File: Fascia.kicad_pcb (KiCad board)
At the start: 6 copper layers, 148.2 x 64.3 mm, 118 parts, among them J1 Verdin iMX95, J10 RTC coin cell, J2 Power in, J3 CAN to ECU, J4 Panel LVDS (provisional), J5 Pre-outs to amp, J6 Mic, J7 USB-C CarPlay, J8 JTAG debug, J9 Buttons, Q1 NFET diode, Q2 NFET pass, Q3 NFET i2c xlat, Q4 NFET i2c xlat, U1 LM74930-Q1, U10 TPS2557-Q1, U2 LM61460-Q1, U3 TLV767-Q1, U4 TCAN1044V-Q1, U5 SN65DSI85-Q1, U6 TLV767-Q1 3V3, U7 SN74AXC4T245-Q1, U8 SN74AXC4T245-Q1, U9 PCM3168A-Q1

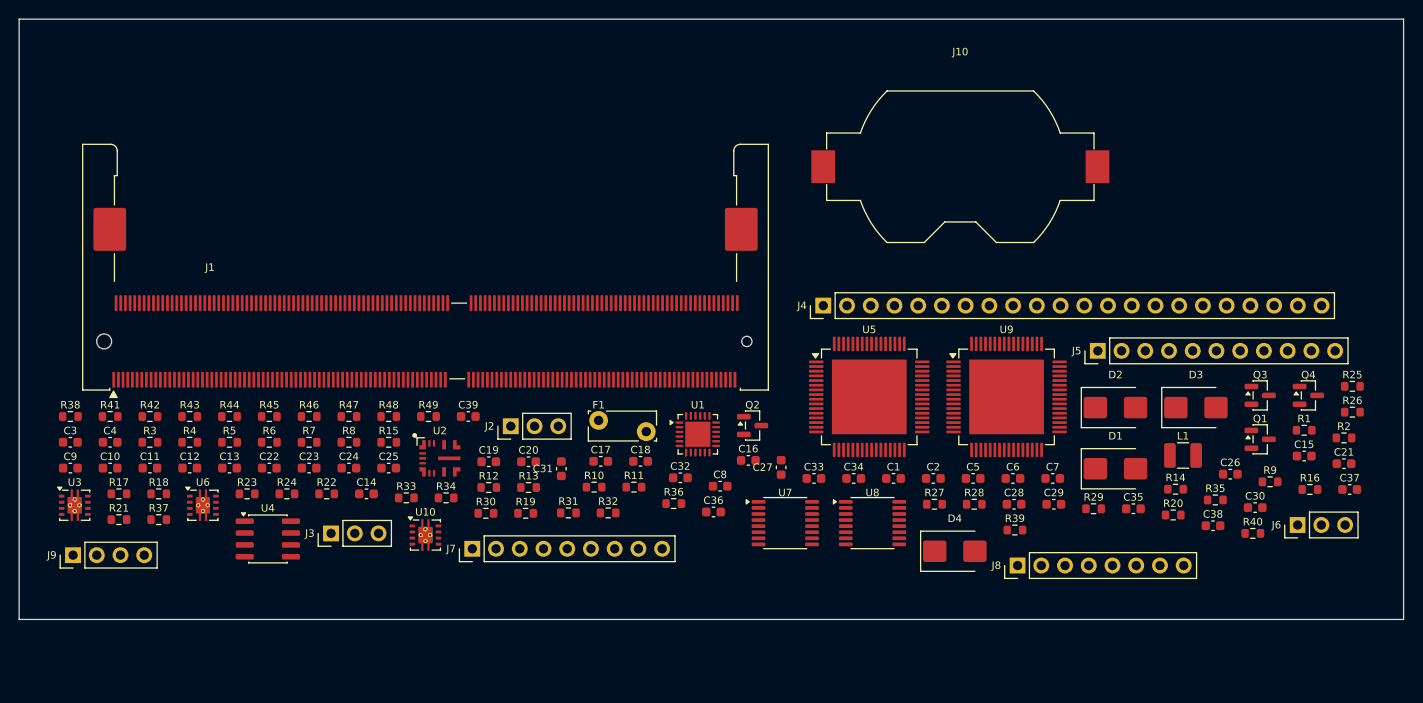
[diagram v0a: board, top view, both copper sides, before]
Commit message: Route Fascia to within 3 connections: bridge beside socket, passives near their IC
Area-ordered skyline placement put the DSI bridge 75 mm from the Verdin
socket and scattered passives far from their ICs (REFCLK_GND resistor 130 mm
from U5). PIN_FIRST places bridge/socket/panel connector first; PULL makes a
passive take the slot nearest its anchor IC. HPWL 7612 -> 5895 mm; FreeRouting
at 12 passes 22 -> 4 unrouted. CLEAR 1.3 -> 2.0.

150-pass run leaves 3 open (AOUT_RL_N, U9_ADR1_TIE, LVDS_A_Y0N), confirmed by
kicad-cli DRC. route_board.py now streams FreeRouting output to a log, reports
pair skew, and words its warning by whether FreeRouting agreed with DRC.

Co-Authored-By: Claude Sonnet 5.5 <noreply@anthropic.com>
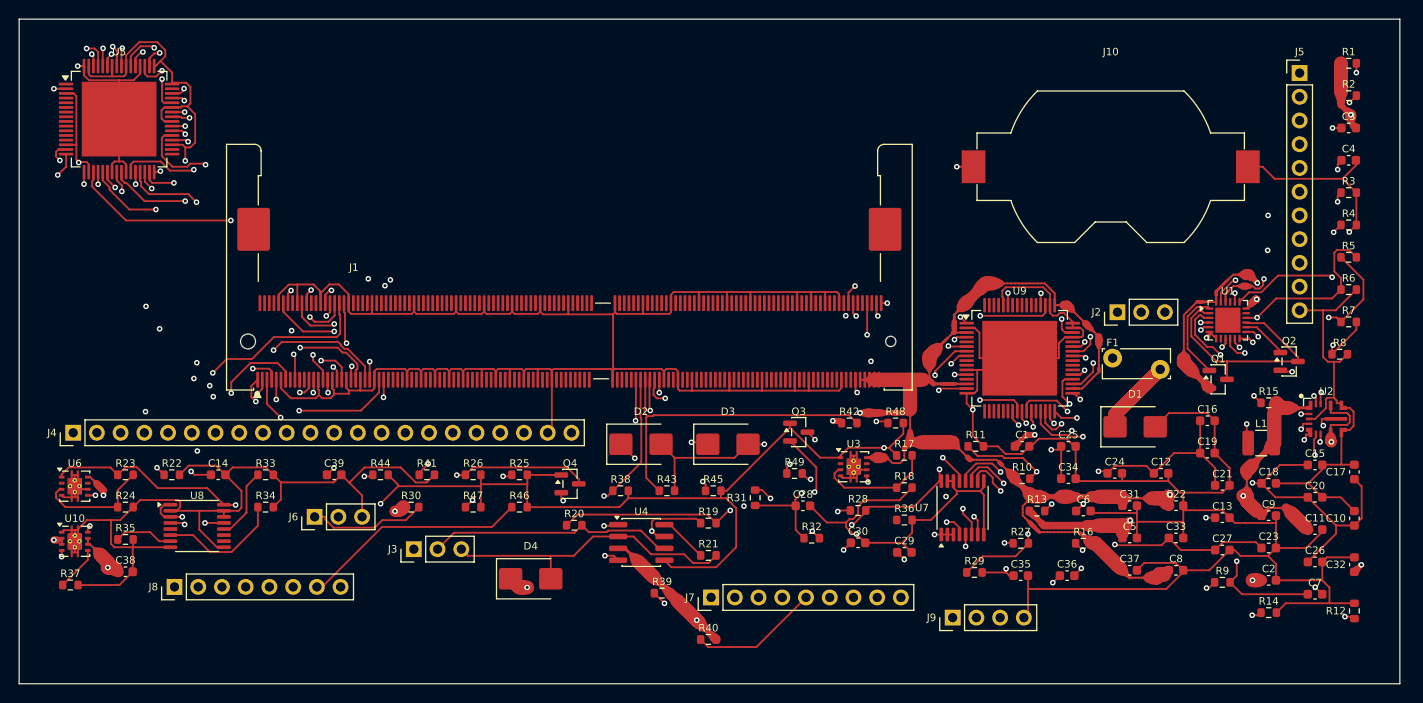
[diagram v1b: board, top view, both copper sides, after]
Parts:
- moved C3 140.9 mm to (142.3, 11.7)
- moved C4 136.0 mm to (142.3, 15.1)
- moved C10 133.3 mm to (142.9, 53.4), turned to 90 degrees
- moved R3 131.1 mm to (142.3, 18.6)
- moved C9 128.4 mm to (133.8, 53.1)
- moved R4 126.2 mm to (142.3, 22.0)
- moved C11 124.9 mm to (138.7, 54.6)
- moved R5 121.4 mm to (142.3, 25.5)
- moved R35 116.7 mm to (11.4, 55.7)
- moved R6 116.7 mm to (142.3, 28.9)
- moved C38 116.5 mm to (11.4, 59.2)
- moved R7 112.0 mm to (142.3, 32.4)
- moved R8 106.5 mm to (141.4, 35.9)
- moved C13 106.4 mm to (128.8, 53.4)
- moved J6 105.2 mm to (31.6, 53.3)
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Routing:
- net GND: track 0.00 -> 895.0 mm, vias 0 -> 7
- net +1V8: track 0.00 -> 325.7 mm, vias 0 -> 10
- net +5V: track 0.00 -> 297.6 mm, vias 0 -> 8
- net +3V3: track 0.00 -> 197.6 mm, vias 0 -> 8
- net RESET_MICO: track 0.00 -> 139.4 mm, vias 0 -> 1
- net VBAT_F: track 0.00 -> 112.1 mm, vias 0 -> 5
- net PWR_EN_MOCI: track 0.00 -> 106.7 mm, vias 0 -> 3
- net PWR_BTN: track 0.00 -> 104.8 mm, vias 0 -> 3
- net CODEC_DOUT_3V3: track 0.00 -> 103.1 mm, vias 0 -> 3
- net USB_VBUS: track 0.00 -> 102.5 mm, vias 0 -> 3
- net JTAG_VREF: track 0.00 -> 100.7 mm, vias 0 -> 2
- net MIC_BIAS_P: track 0.00 -> 95.9 mm, vias 0 -> 1
- net MIC_IN_N: track 0.00 -> 92.8 mm, vias 0 -> 2
- net +12V_PROT: track 0.00 -> 87.8 mm, vias 0 -> 4
- net I2S_BCK_1V8: track 0.00 -> 87.5 mm, vias 0 -> 3
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- added copper zone on In1.Cu, net GND
- added copper zone on In4.Cu, net GND
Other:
- board size 148.2 x 64.3 mm -> 147.8 x 71.1 mm
